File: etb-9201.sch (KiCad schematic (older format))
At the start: 5 parts, among them U1201 TLE9201SG

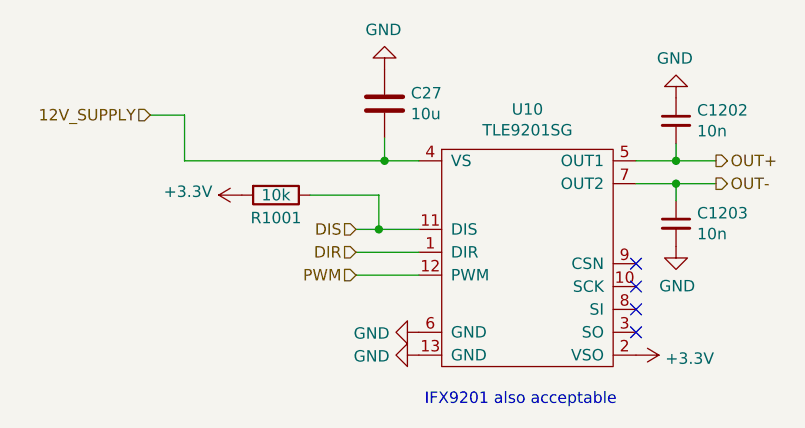
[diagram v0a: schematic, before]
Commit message: switch to SN74LVC2G17 #122
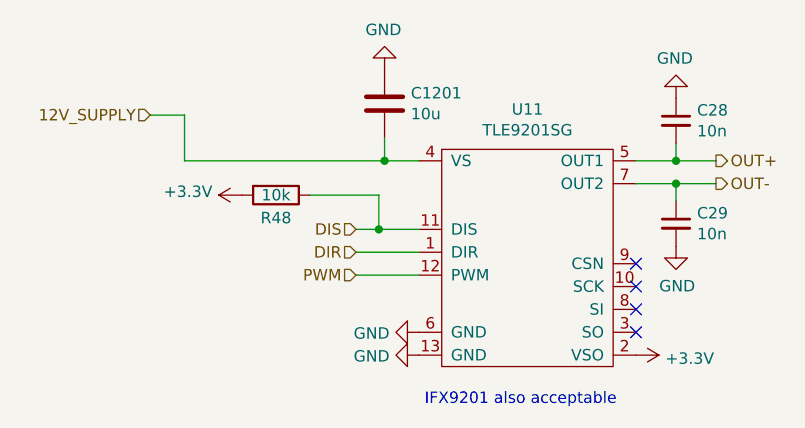
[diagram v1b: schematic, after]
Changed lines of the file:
@@
 AR Path="/62471BCF/5DD47E93" Ref="U10"  Part="1"
 AR Path="/6247AE9A/5DD47E93" Ref="U11"  Part="1"
-F 0 "U10" H 2850 2325 50  0000 C CNN
+F 0 "U11" H 2850 2325 50  0000 C CNN
 F 1 "TLE9201SG" H 2850 2234 50  0000 C CNN
 F 2 "Package_SO:Infineon_PG-DSO-12-9" H 2725 1750 50  0001 C CNN
@@
 AR Path="/62471BCF/5DD48EC1" Ref="C1202"  Part="1"
 AR Path="/6247AE9A/5DD48EC1" Ref="C28"  Part="1"
-F 0 "C1202" H 3592 1171 50  0000 L CNN
+F 0 "C28" H 3592 1171 50  0000 L CNN
 F 1 "10n" H 3592 1080 50  0000 L CNN
 F 2 "Capacitor_SMD:C_0603_1608Metric" H 3500 1125 50  0001 C CNN
@@
 AR Path="/62471BCF/5DD49883" Ref="C1203"  Part="1"
 AR Path="/6247AE9A/5DD49883" Ref="C29"  Part="1"
-F 0 "C1203" H 3592 1621 50  0000 L CNN
+F 0 "C29" H 3592 1621 50  0000 L CNN
 F 1 "10n" H 3592 1530 50  0000 L CNN
 F 2 "Capacitor_SMD:C_0603_1608Metric" H 3500 1575 50  0001 C CNN
@@
 AR Path="/62471BCF/5DD4C345" Ref="C27"  Part="1"
 AR Path="/6247AE9A/5DD4C345" Ref="C1201"  Part="1"
-F 0 "C27" H 2340 1096 50  0000 L CNN
+F 0 "C1201" H 2340 1096 50  0000 L CNN
 F 1 "10u" H 2340 1005 50  0000 L CNN
 F 2 "Capacitor_SMD:C_1206_3216Metric" H 2263 900 50  0001 C CNN
@@
 AR Path="/62471BCF/5DF25274" Ref="R1001"  Part="1"
 AR Path="/6247AE9A/5DF25274" Ref="R48"  Part="1"
-F 0 "R1001" V 1850 1450 50  0000 C CNN
+F 0 "R48" V 1850 1450 50  0000 C CNN
 F 1 "10k" V 1750 1450 50  0000 C CNN
 F 2 "Resistor_SMD:R_0402_1005Metric" V 1680 1450 50  0001 C CNN
